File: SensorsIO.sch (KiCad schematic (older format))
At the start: 11 parts, among them J3 Conn_01x10_Male, J4 Conn_01x04_Male, J5 Conn_01x04_Male

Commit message: Se Organiza conexiones de alimentacion con elementos de la biblioteca power, se quitan algunas etiquetas y se coloca la fuente en hoja principal
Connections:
- net labels added: +3.3V, +5V
- net labels removed: +3V3, +5V0
- wire segments 17 -> 18
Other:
- moved on the sheet: D4, J3, J4, J5, R10, R11, R7, R8, R9, RV1

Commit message: Se agregan recomendaciones izq->dcha (In/Out), se Reorganiza jerarquía y bus de datos, se coloca graphics lines para indicar submodulos
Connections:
- wire segments 18 -> 22
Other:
- moved on the sheet: R5, RV1
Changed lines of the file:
@@
 AR Path="/5CCF7078/5CE24118" Ref="R?"  Part="1"
 AR Path="/5CCF6F7E/5CE24118" Ref="R7"  Part="1"
-F 0 "R7" H 5820 2946 50  0000 L CNN
+AR Path="/5D002D0B/5CE24118" Ref="R1"  Part="1"
+AR Path="/5D086332/5CE24118" Ref="R?"  Part="1"
+F 0 "R1" H 5820 2946 50  0000 L CNN
 F 1 "330" H 5820 2855 50  0000 L CNN
 F 2 "" V 5680 2900 50  0001 C CNN
@@
 AR Path="/5CCF7078/5CE2411E" Ref="D?"  Part="1"
 AR Path="/5CCF6F7E/5CE2411E" Ref="D4"  Part="1"
+AR Path="/5D002D0B/5CE2411E" Ref="D4"  Part="1"
+AR Path="/5D086332/5CE2411E" Ref="D?"  Part="1"
 F 0 "D4" V 5789 3183 50  0000 R CNN
 F 1 "LED" V 5698 3183 50  0000 R CNN
@@
 U 1 1 5CE249B8
 P 6700 3350
+AR Path="/5CCF6F7E/5CE249B8" Ref="D5"  Part="1"
+AR Path="/5D002D0B/5CE249B8" Ref="D5"  Part="1"
+AR Path="/5D086332/5CE249B8" Ref="D?"  Part="1"
 F 0 "D5" V 6746 3020 50  0000 R CNN
 F 1 "LED_RGB" V 6655 3020 50  0000 R CNN
@@
 U 1 1 5CE27928
 P 3500 3600
+AR Path="/5CCF6F7E/5CE27928" Ref="J4"  Part="1"
+AR Path="/5D002D0B/5CE27928" Ref="J4"  Part="1"
+AR Path="/5D086332/5CE27928" Ref="J?"  Part="1"
 F 0 "J4" H 3472 3482 50  0000 R CNN
 F 1 "Conn_01x04_Male" V 3250 3800 50  0000 R CNN
@@
 $EndComp
 $Comp
-L Device:R_POT RV1
-U 1 1 5CE29D0F
-P 8250 3350
-F 0 "RV1" H 8181 3396 50  0000 R CNN
-F 1 "10K" H 8181 3305 50  0000 R CNN
-F 2 "" H 8250 3350 50  0001 C CNN
-F 3 "~" H 8250 3350 50  0001 C CNN
-	1    8250 3350
-	1    0    0    -1
-$EndComp
-$Comp
 L Connector:Conn_01x04_Male J5
 U 1 1 5CE2B4D2
 P 3500 4150
+AR Path="/5CCF6F7E/5CE2B4D2" Ref="J5"  Part="1"
+AR Path="/5D002D0B/5CE2B4D2" Ref="J5"  Part="1"
+AR Path="/5D086332/5CE2B4D2" Ref="J?"  Part="1"
 F 0 "J5" H 3472 4032 50  0000 R CNN
 F 1 "Conn_01x04_Male" V 3250 4550 50  0000 R CNN
@@
 Text HLabel 5750 2600 0    50   Input ~ 10
 LED_OUT
-Text HLabel 6500 2800 1    50   Input ~ 10
+Text HLabel 6500 2700 1    50   Input ~ 10
 LED_R
-Text HLabel 6700 2800 1    50   Input ~ 10
+Text HLabel 6700 2700 1    50   Input ~ 10
 LED_G
-Text HLabel 6900 2800 1    50   Input ~ 10
+Text HLabel 6900 2700 1    50   Input ~ 10
 LED_B
 Wire Wire Line
@@
 U 1 1 5CE2E82D
 P 6700 3900
-F 0 "#PWR017" H 6700 3650 50  0001 C CNN
+AR Path="/5CCF6F7E/5CE2E82D" Ref="#PWR017"  Part="1"
+AR Path="/5D002D0B/5CE2E82D" Ref="#PWR06"  Part="1"
+AR Path="/5D086332/5CE2E82D" Ref="#PWR?"  Part="1"
+F 0 "#PWR06" H 6700 3650 50  0001 C CNN
 F 1 "GND" H 6705 3727 50  0000 C CNN
 F 2 "" H 6700 3900 50  0001 C CNN
@@
 AR Path="/5CCEA06C/5CE394BD" Ref="R?"  Part="1"
 AR Path="/5CCF6F7E/5CE394BD" Ref="R10"  Part="1"
-F 0 "R10" V 7000 2950 50  0000 L CNN
+AR Path="/5D002D0B/5CE394BD" Ref="R4"  Part="1"
+AR Path="/5D086332/5CE394BD" Ref="R?"  Part="1"
+F 0 "R4" V 7000 2950 50  0000 L CNN
 F 1 "330" V 7000 2750 50  0000 L CNN
 F 2 "" V 6830 2950 50  0001 C CNN
@@
 AR Path="/5CCEA06C/5CE394C3" Ref="R?"  Part="1"
 AR Path="/5CCF6F7E/5CE394C3" Ref="R9"  Part="1"
-F 0 "R9" V 6600 2950 50  0000 L CNN
+AR Path="/5D002D0B/5CE394C3" Ref="R3"  Part="1"
+AR Path="/5D086332/5CE394C3" Ref="R?"  Part="1"
+F 0 "R3" V 6600 2950 50  0000 L CNN
 F 1 "330" V 6600 2750 50  0000 L CNN
 F 2 "" V 6630 2950 50  0001 C CNN
@@
 AR Path="/5CCEA06C/5CE394C9" Ref="R?"  Part="1"
 AR Path="/5CCF6F7E/5CE394C9" Ref="R8"  Part="1"
-F 0 "R8" V 6400 2950 50  0000 L CNN
+AR Path="/5D002D0B/5CE394C9" Ref="R2"  Part="1"
+AR Path="/5D086332/5CE394C9" Ref="R?"  Part="1"
+F 0 "R2" V 6400 2950 50  0000 L CNN
 F 1 "330" V 6400 2750 50  0000 L CNN
 F 2 "" V 6430 2950 50  0001 C CNN
@@
 U 1 1 5CE3F7BF
 P 5750 3650
-F 0 "#PWR016" H 5750 3400 50  0001 C CNN
+AR Path="/5CCF6F7E/5CE3F7BF" Ref="#PWR016"  Part="1"
+AR Path="/5D002D0B/5CE3F7BF" Ref="#PWR05"  Part="1"
+AR Path="/5D086332/5CE3F7BF" Ref="#PWR?"  Part="1"
+F 0 "#PWR05" H 5750 3400 50  0001 C CNN
 F 1 "GND" H 5755 3477 50  0000 C CNN
 F 2 "" H 5750 3650 50  0001 C CNN
@@
 Wire Wire Line
 	5750 3450 5750 3650
-Text HLabel 8550 3350 2    50   Input ~ 10
-POT
-Wire Wire Line
-	8550 3350 8400 3350
-$Comp
-L power:GND #PWR018
-U 1 1 5CE41733
-P 8250 3850
-F 0 "#PWR018" H 8250 3600 50  0001 C CNN
-F 1 "GND" H 8255 3677 50  0000 C CNN
-F 2 "" H 8250 3850 50  0001 C CNN
-F 3 "" H 8250 3850 50  0001 C CNN
-	1    8250 3850
-	1    0    0    -1
-$EndComp
-$Comp
-L Device:R R11
-U 1 1 5CE41EFC
-P 8250 3650
-F 0 "R11" H 8320 3696 50  0000 L CNN
-F 1 "1K" H 8320 3605 50  0000 L CNN
-F 2 "" V 8180 3650 50  0001 C CNN
-F 3 "~" H 8250 3650 50  0001 C CNN
-	1    8250 3650
-	1    0    0    -1
-$EndComp
-Wire Wire Line
-	8250 3850 8250 3800
 Text HLabel 3300 4150 0    50   Input ~ 10
 IO_D10
-Wire Wire Line
-	8250 2400 8250 3200
 $Comp
 L Connector:Conn_01x10_Male J3
 U 1 1 5CE5D9BC
 P 3500 2650
+AR Path="/5CCF6F7E/5CE5D9BC" Ref="J3"  Part="1"
+AR Path="/5D002D0B/5CE5D9BC" Ref="J3"  Part="1"
+AR Path="/5D086332/5CE5D9BC" Ref="J?"  Part="1"
 F 0 "J3" H 3472 2624 50  0000 R CNN
 F 1 "Conn_01x10_Male" V 3250 2950 50  0000 R CNN
@@
 U 1 1 5CE63A36
 P 3200 3150
-F 0 "#PWR015" H 3200 2900 50  0001 C CNN
+AR Path="/5CCF6F7E/5CE63A36" Ref="#PWR015"  Part="1"
+AR Path="/5D002D0B/5CE63A36" Ref="#PWR04"  Part="1"
+AR Path="/5D086332/5CE63A36" Ref="#PWR?"  Part="1"
+F 0 "#PWR04" H 3200 2900 50  0001 C CNN
 F 1 "GND" V 3205 3022 50  0000 R CNN
 F 2 "" H 3200 3150 50  0001 C CNN
@@
 U 1 1 5CF63594
 P 3200 3050
-F 0 "#PWR0117" H 3200 2900 50  0001 C CNN
+AR Path="/5CCF6F7E/5CF63594" Ref="#PWR0117"  Part="1"
+AR Path="/5D002D0B/5CF63594" Ref="#PWR03"  Part="1"
+AR Path="/5D086332/5CF63594" Ref="#PWR?"  Part="1"
+F 0 "#PWR03" H 3200 2900 50  0001 C CNN
 F 1 "+5V" V 3215 3178 50  0000 L CNN
 F 2 "" H 3200 3050 50  0001 C CNN
@@
 U 1 1 5CF63D38
 P 3200 2950
-F 0 "#PWR0118" H 3200 2800 50  0001 C CNN
+AR Path="/5CCF6F7E/5CF63D38" Ref="#PWR0118"  Part="1"
+AR Path="/5D002D0B/5CF63D38" Ref="#PWR02"  Part="1"
+AR Path="/5D086332/5CF63D38" Ref="#PWR?"  Part="1"
+F 0 "#PWR02" H 3200 2800 50  0001 C CNN
 F 1 "+3.3V" V 3215 3078 50  0000 L CNN
 F 2 "" H 3200 2950 50  0001 C CNN
@@
 	0    -1   -1   0
 $EndComp
+Wire Wire Line
+	3200 3150 3300 3150
+Wire Wire Line
+	5750 2600 5750 2750
+Wire Wire Line
+	8100 3400 8100 3250
 $Comp
 L power:VDD #PWR0119
 U 1 1 5CF66350
-P 8250 2400
-F 0 "#PWR0119" H 8250 2250 50  0001 C CNN
-F 1 "VDD" H 8267 2573 50  0000 C CNN
-F 2 "" H 8250 2400 50  0001 C CNN
-F 3 "" H 8250 2400 50  0001 C CNN
-	1    8250 2400
-	1    0    0    -1
-$EndComp
-Wire Wire Line
-	3200 3150 3300 3150
-Wire Wire Line
-	5750 2600 5750 2750
+P 8100 2650
+AR Path="/5CCF6F7E/5CF66350" Ref="#PWR0119"  Part="1"
+AR Path="/5D002D0B/5CF66350" Ref="#PWR07"  Part="1"
+AR Path="/5D086332/5CF66350" Ref="#PWR?"  Part="1"
+F 0 "#PWR07" H 8100 2500 50  0001 C CNN
+F 1 "VDD" H 8117 2823 50  0000 C CNN
+F 2 "" H 8100 2650 50  0001 C CNN
+F 3 "" H 8100 2650 50  0001 C CNN
+	1    8100 2650
+	1    0    0    -1
+$EndComp
+Wire Wire Line
+	8100 2650 8100 2950
+Wire Wire Line
+	8100 3750 8100 3700
+$Comp
+L Device:R R11
+U 1 1 5CE41EFC
+P 8100 3550
+AR Path="/5CCF6F7E/5CE41EFC" Ref="R11"  Part="1"
+AR Path="/5D002D0B/5CE41EFC" Ref="R5"  Part="1"
+AR Path="/5D086332/5CE41EFC" Ref="R?"  Part="1"
+F 0 "R5" H 8170 3596 50  0000 L CNN
+F 1 "1K" H 8170 3505 50  0000 L CNN
+F 2 "" V 8030 3550 50  0001 C CNN
+F 3 "~" H 8100 3550 50  0001 C CNN
+	1    8100 3550
+	1    0    0    -1
+$EndComp
+$Comp
+L power:GND #PWR018
+U 1 1 5CE41733
+P 8100 3750
+AR Path="/5CCF6F7E/5CE41733" Ref="#PWR018"  Part="1"
+AR Path="/5D002D0B/5CE41733" Ref="#PWR08"  Part="1"
+AR Path="/5D086332/5CE41733" Ref="#PWR?"  Part="1"
+F 0 "#PWR08" H 8100 3500 50  0001 C CNN
+F 1 "GND" H 8105 3577 50  0000 C CNN
+F 2 "" H 8100 3750 50  0001 C CNN
+F 3 "" H 8100 3750 50  0001 C CNN
+	1    8100 3750
+	1    0    0    -1
+$EndComp
+Wire Wire Line
+	8400 3100 8250 3100
+Text HLabel 8400 3100 2    50   Input ~ 10
+POT
+$Comp
+L Device:R_POT RV1
+U 1 1 5CE29D0F
+P 8100 3100
+AR Path="/5CCF6F7E/5CE29D0F" Ref="RV1"  Part="1"
+AR Path="/5D002D0B/5CE29D0F" Ref="RV1"  Part="1"
+AR Path="/5D086332/5CE29D0F" Ref="RV?"  Part="1"
+F 0 "RV1" H 8031 3146 50  0000 R CNN
+F 1 "10K" H 8031 3055 50  0000 R CNN
+F 2 "" H 8100 3100 50  0001 C CNN
+F 3 "~" H 8100 3100 50  0001 C CNN
+	1    8100 3100
+	1    0    0    -1
+$EndComp
+Wire Wire Line
+	6500 2700 6500 2800
+Wire Wire Line
+	6700 2800 6700 2700
+Wire Wire Line
+	6900 2800 6900 2700
 $EndSCHEMATC

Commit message: Se agrega ubicación de componentes, asociación de footprint, pendiente Ruteo.
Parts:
- removed D5: LED_RGB, symbol Device:LED_RGB
- added D5: LED_CRGB, LED_SMD:LED_RGB_1210, symbol Device:LED_CRGB
- D4: footprint (none) -> LED_SMD:LED_0603_1608Metric_Castellated; Part number (none) -> 160-1447-1-ND
- J3: footprint (none) -> Connector_PinSocket_2.54mm:PinSocket_1x10_P2.54mm_Vertical
- J4, J5: footprint (none) -> Connector_PinSocket_2.54mm:PinSocket_1x04_P2.54mm_Vertical
- R10, R11, R7, R8, R9: footprint (none) -> Resistor_SMD:R_0603_1608Metric_Pad1.05x0.95mm_HandSolder
- RV1: footprint (none) -> Potentiometer_THT:Potentiometer_Alps_RK09K_Single_Vertical; Part Number (none) -> 987-1305-ND
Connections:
- wire segments 22 -> 17
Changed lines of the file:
@@
 F 0 "R1" H 5820 2946 50  0000 L CNN
 F 1 "330" H 5820 2855 50  0000 L CNN
-F 2 "" V 5680 2900 50  0001 C CNN
+F 2 "Resistor_SMD:R_0603_1608Metric_Pad1.05x0.95mm_HandSolder" V 5680 2900 50  0001 C CNN
 F 3 "~" H 5750 2900 50  0001 C CNN
 	1    5750 2900
@@
 F 0 "D4" V 5789 3183 50  0000 R CNN
 F 1 "LED" V 5698 3183 50  0000 R CNN
-F 2 "" H 5750 3300 50  0001 C CNN
+F 2 "LED_SMD:LED_0603_1608Metric_Castellated" H 5750 3300 50  0001 C CNN
 F 3 "~" H 5750 3300 50  0001 C CNN
+F 4 "160-1447-1-ND" V 5750 3300 50  0001 C CNN "Part number"
 	1    5750 3300
-	0    -1   -1   0
-$EndComp
-$Comp
-L Device:LED_RGB D5
-U 1 1 5CE249B8
-P 6700 3350
-AR Path="/5CCF6F7E/5CE249B8" Ref="D5"  Part="1"
-AR Path="/5D002D0B/5CE249B8" Ref="D5"  Part="1"
-AR Path="/5D086332/5CE249B8" Ref="D?"  Part="1"
-F 0 "D5" V 6746 3020 50  0000 R CNN
-F 1 "LED_RGB" V 6655 3020 50  0000 R CNN
-F 2 "" H 6700 3300 50  0001 C CNN
-F 3 "~" H 6700 3300 50  0001 C CNN
-	1    6700 3350
 	0    -1   -1   0
 $EndComp
@@
 F 0 "J4" H 3472 3482 50  0000 R CNN
 F 1 "Conn_01x04_Male" V 3250 3800 50  0000 R CNN
-F 2 "" H 3500 3600 50  0001 C CNN
+F 2 "Connector_PinSocket_2.54mm:PinSocket_1x04_P2.54mm_Vertical" H 3500 3600 50  0001 C CNN
 F 3 "~" H 3500 3600 50  0001 C CNN
 	1    3500 3600
@@
 F 0 "J5" H 3472 4032 50  0000 R CNN
 F 1 "Conn_01x04_Male" V 3250 4550 50  0000 R CNN
-F 2 "" H 3500 4150 50  0001 C CNN
+F 2 "Connector_PinSocket_2.54mm:PinSocket_1x04_P2.54mm_Vertical" H 3500 4150 50  0001 C CNN
 F 3 "~" H 3500 4150 50  0001 C CNN
 	1    3500 4150
@@
 Text HLabel 6900 2700 1    50   Input ~ 10
 LED_B
-Wire Wire Line
-	6500 3700 6700 3700
-Wire Wire Line
-	6700 3700 6700 3550
-Wire Wire Line
-	6900 3550 6900 3700
-Wire Wire Line
-	6900 3700 6700 3700
-Connection ~ 6700 3700
-Wire Wire Line
-	6500 3550 6500 3700
 $Comp
 L power:GND #PWR017
@@
 	1    0    0    -1
 $EndComp
-Wire Wire Line
-	6700 3700 6700 3900
 $Comp
 L Device:R R?
@@
 F 0 "R4" V 7000 2950 50  0000 L CNN
 F 1 "330" V 7000 2750 50  0000 L CNN
-F 2 "" V 6830 2950 50  0001 C CNN
+F 2 "Resistor_SMD:R_0603_1608Metric_Pad1.05x0.95mm_HandSolder" V 6830 2950 50  0001 C CNN
 F 3 "~" H 6900 2950 50  0001 C CNN
 	1    6900 2950
@@
 F 0 "R3" V 6600 2950 50  0000 L CNN
 F 1 "330" V 6600 2750 50  0000 L CNN
-F 2 "" V 6630 2950 50  0001 C CNN
+F 2 "Resistor_SMD:R_0603_1608Metric_Pad1.05x0.95mm_HandSolder" V 6630 2950 50  0001 C CNN
 F 3 "~" H 6700 2950 50  0001 C CNN
 	1    6700 2950
@@
 F 0 "R2" V 6400 2950 50  0000 L CNN
 F 1 "330" V 6400 2750 50  0000 L CNN
-F 2 "" V 6430 2950 50  0001 C CNN
+F 2 "Resistor_SMD:R_0603_1608Metric_Pad1.05x0.95mm_HandSolder" V 6430 2950 50  0001 C CNN
 F 3 "~" H 6500 2950 50  0001 C CNN
 	1    6500 2950
 	1    0    0    -1
 $EndComp
-Wire Wire Line
-	6900 3150 6900 3100
-Wire Wire Line
-	6700 3150 6700 3100
-Wire Wire Line
-	6500 3150 6500 3100
 $Comp
 L power:GND #PWR016
@@
 F 0 "J3" H 3472 2624 50  0000 R CNN
 F 1 "Conn_01x10_Male" V 3250 2950 50  0000 R CNN
-F 2 "" H 3500 2650 50  0001 C CNN
+F 2 "Connector_PinSocket_2.54mm:PinSocket_1x10_P2.54mm_Vertical" H 3500 2650 50  0001 C CNN
 F 3 "~" H 3500 2650 50  0001 C CNN
 	1    3500 2650
@@
 F 0 "R5" H 8170 3596 50  0000 L CNN
 F 1 "1K" H 8170 3505 50  0000 L CNN
-F 2 "" V 8030 3550 50  0001 C CNN
+F 2 "Resistor_SMD:R_0603_1608Metric_Pad1.05x0.95mm_HandSolder" V 8030 3550 50  0001 C CNN
 F 3 "~" H 8100 3550 50  0001 C CNN
 	1    8100 3550
@@
 F 0 "RV1" H 8031 3146 50  0000 R CNN
 F 1 "10K" H 8031 3055 50  0000 R CNN
-F 2 "" H 8100 3100 50  0001 C CNN
+F 2 "Potentiometer_THT:Potentiometer_Alps_RK09K_Single_Vertical" H 8100 3100 50  0001 C CNN
 F 3 "~" H 8100 3100 50  0001 C CNN
+F 4 "987-1305-ND" H 8100 3100 50  0001 C CNN "Part Number"
 	1    8100 3100
 	1    0    0    -1
@@
 Wire Wire Line
 	6900 2800 6900 2700
+$Comp
+L Device:LED_CRGB D5
+U 1 1 5CF74075
+P 6700 3500
+F 0 "D5" V 6746 3170 50  0000 R CNN
+F 1 "LED_CRGB" V 6655 3170 50  0000 R CNN
+F 2 "LED_SMD:LED_RGB_1210" H 6700 3450 50  0001 C CNN
+F 3 "~" H 6700 3450 50  0001 C CNN
+F 4 "	516-1778-6-ND" V 6700 3500 50  0001 C CNN "Part Number"
+	1    6700 3500
+	0    -1   -1   0
+$EndComp
+Wire Wire Line
+	6500 3100 6500 3300
+Wire Wire Line
+	6700 3100 6700 3300
+Wire Wire Line
+	6900 3100 6900 3300
+Wire Wire Line
+	6700 3900 6700 3700
 $EndSCHEMATC

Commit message: Se reorganiza componenentes lineas mas limpias y analógicas mas cerca,Se cambia potenciometro y bornera de alimentación, se colocan perforaciones en la tarjeta
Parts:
- RV1: footprint Potentiometer_THT:Potentiometer_Alps_RK09K_Single_Vertical -> Potentiometer_SMD:Potentiometer_ACP_CA6-VSMD_Vertical
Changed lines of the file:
@@
 F 0 "RV1" H 8031 3146 50  0000 R CNN
 F 1 "10K" H 8031 3055 50  0000 R CNN
-F 2 "Potentiometer_THT:Potentiometer_Alps_RK09K_Single_Vertical" H 8100 3100 50  0001 C CNN
+F 2 "Potentiometer_SMD:Potentiometer_ACP_CA6-VSMD_Vertical" H 8100 3100 50  0001 C CNN
 F 3 "~" H 8100 3100 50  0001 C CNN
 F 4 "987-1305-ND" H 8100 3100 50  0001 C CNN "Part Number"

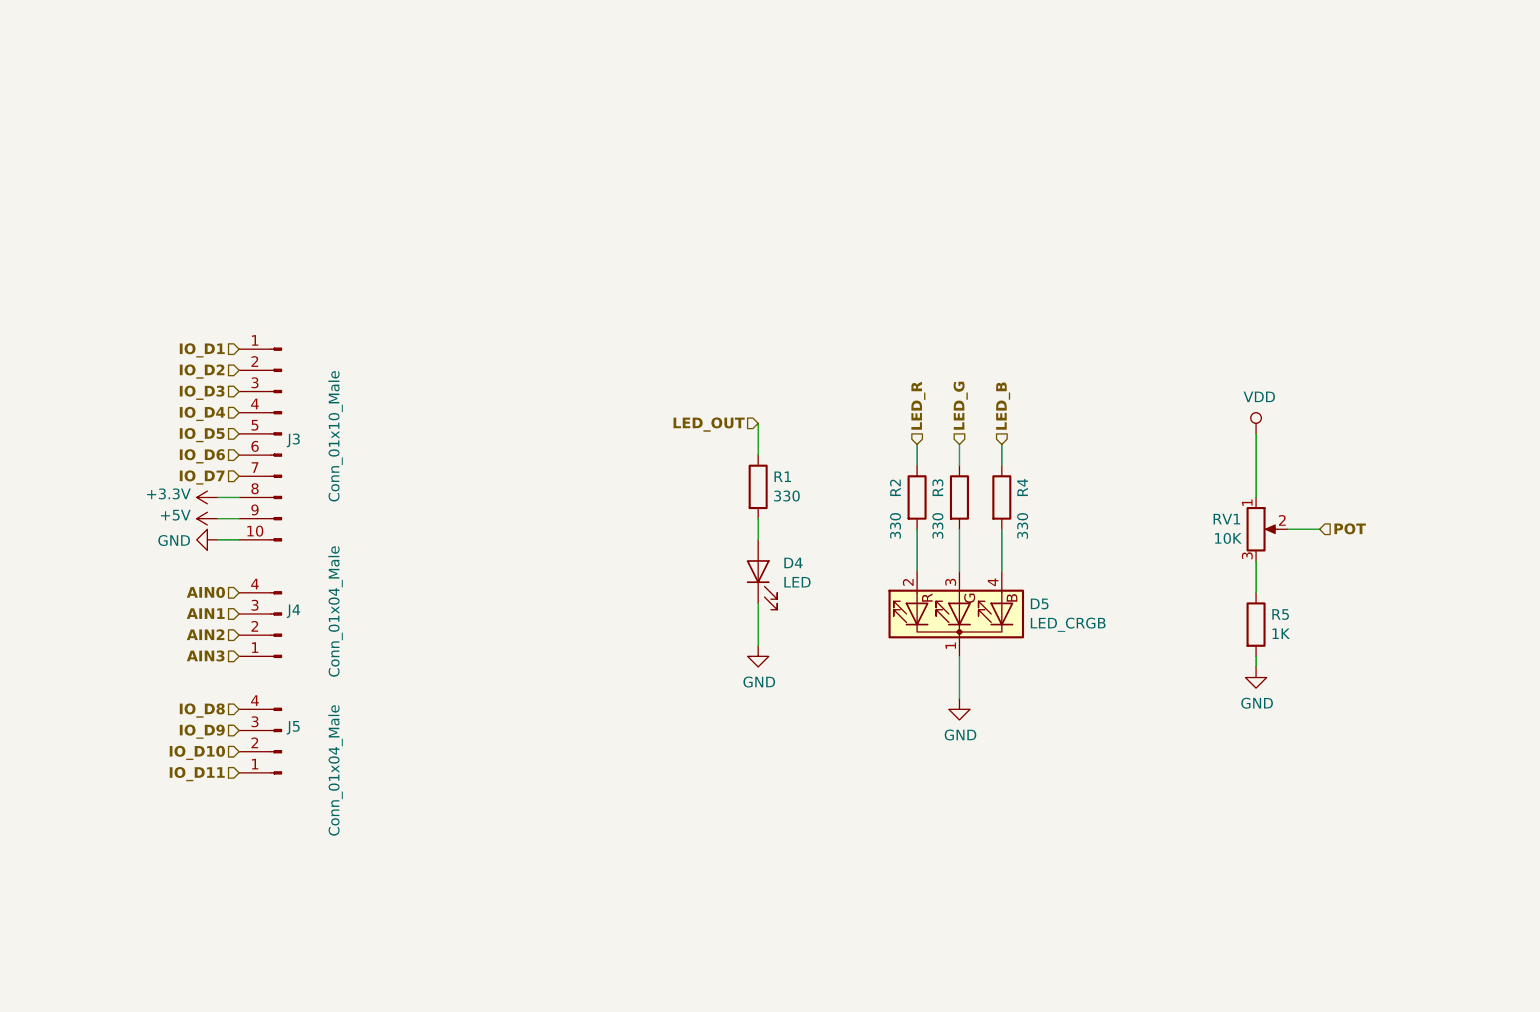
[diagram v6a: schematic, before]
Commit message: Se agrega info del circuito,prolijidad en conexiones  se corrije,ERC Warninsg no errores,pendinete Datasheet y algunos numeros de parte,Comentario esquematico1: no es necesario con los labels que esta considero que esta ok, componentes los dejo en 0603, grilla en pcb 0.127 mm a criterio propio, se colocan fiduciales, pendiente lo demas de PCB.
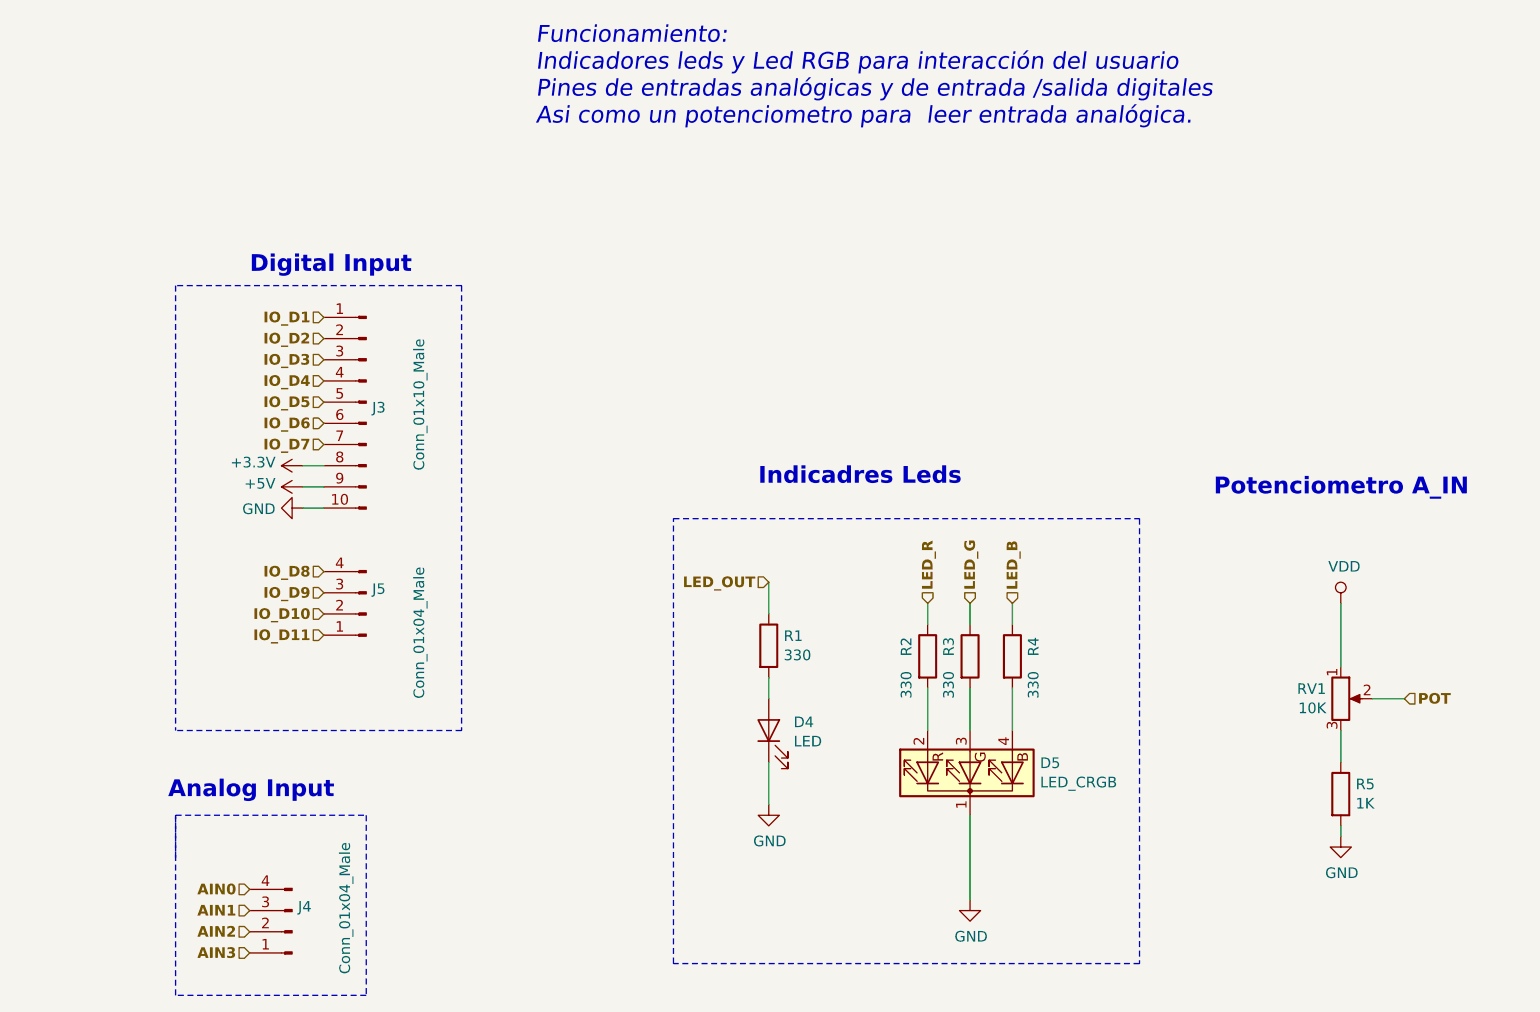
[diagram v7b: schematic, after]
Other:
- note added: "Analog Input"
- note added: "Digital Input"
- note added: "Funcionamiento:\nIndicadores leds y Led RGB para interacción del usuario\nPines de entradas analógicas y de entrada /salida digitales\nAsi como un potenciometro para leer entrada analógica."
- note added: "Indicadres Leds"
- note added: "Potenciometro A_IN"
- moved on the sheet: D4, D5, J3, J4, J5, R1, R2, R3, R4, R5, RV1
